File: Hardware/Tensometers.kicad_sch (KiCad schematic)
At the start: 27 parts, among them IC1 MCP1501T-18E_CHY, U24 AD8226BRMZ-R7, U31 MCP6002-xMC, U33 MCP6002-xMC, U34 AD8226BRMZ-R7, U35 AD8226BRMZ-R7, U36 AD8226BRMZ-R7

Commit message: Frontbox 2025 Version 1.0
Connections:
- net 12V1 renamed +12V

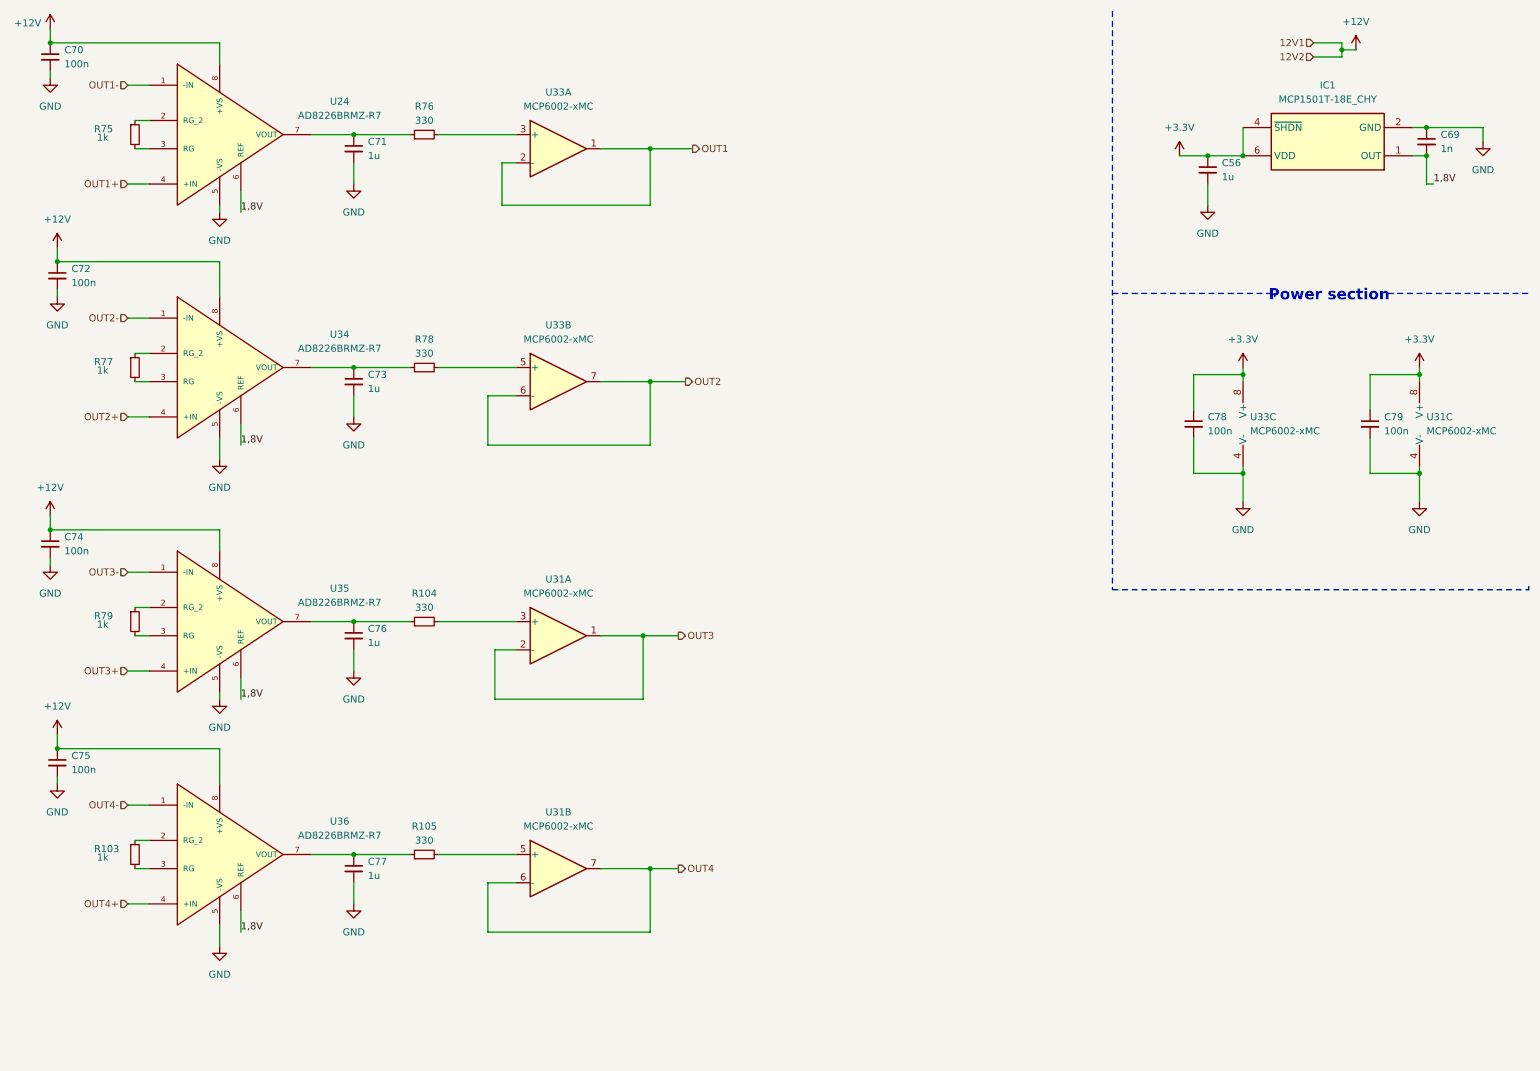
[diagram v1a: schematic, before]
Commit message: Converter change
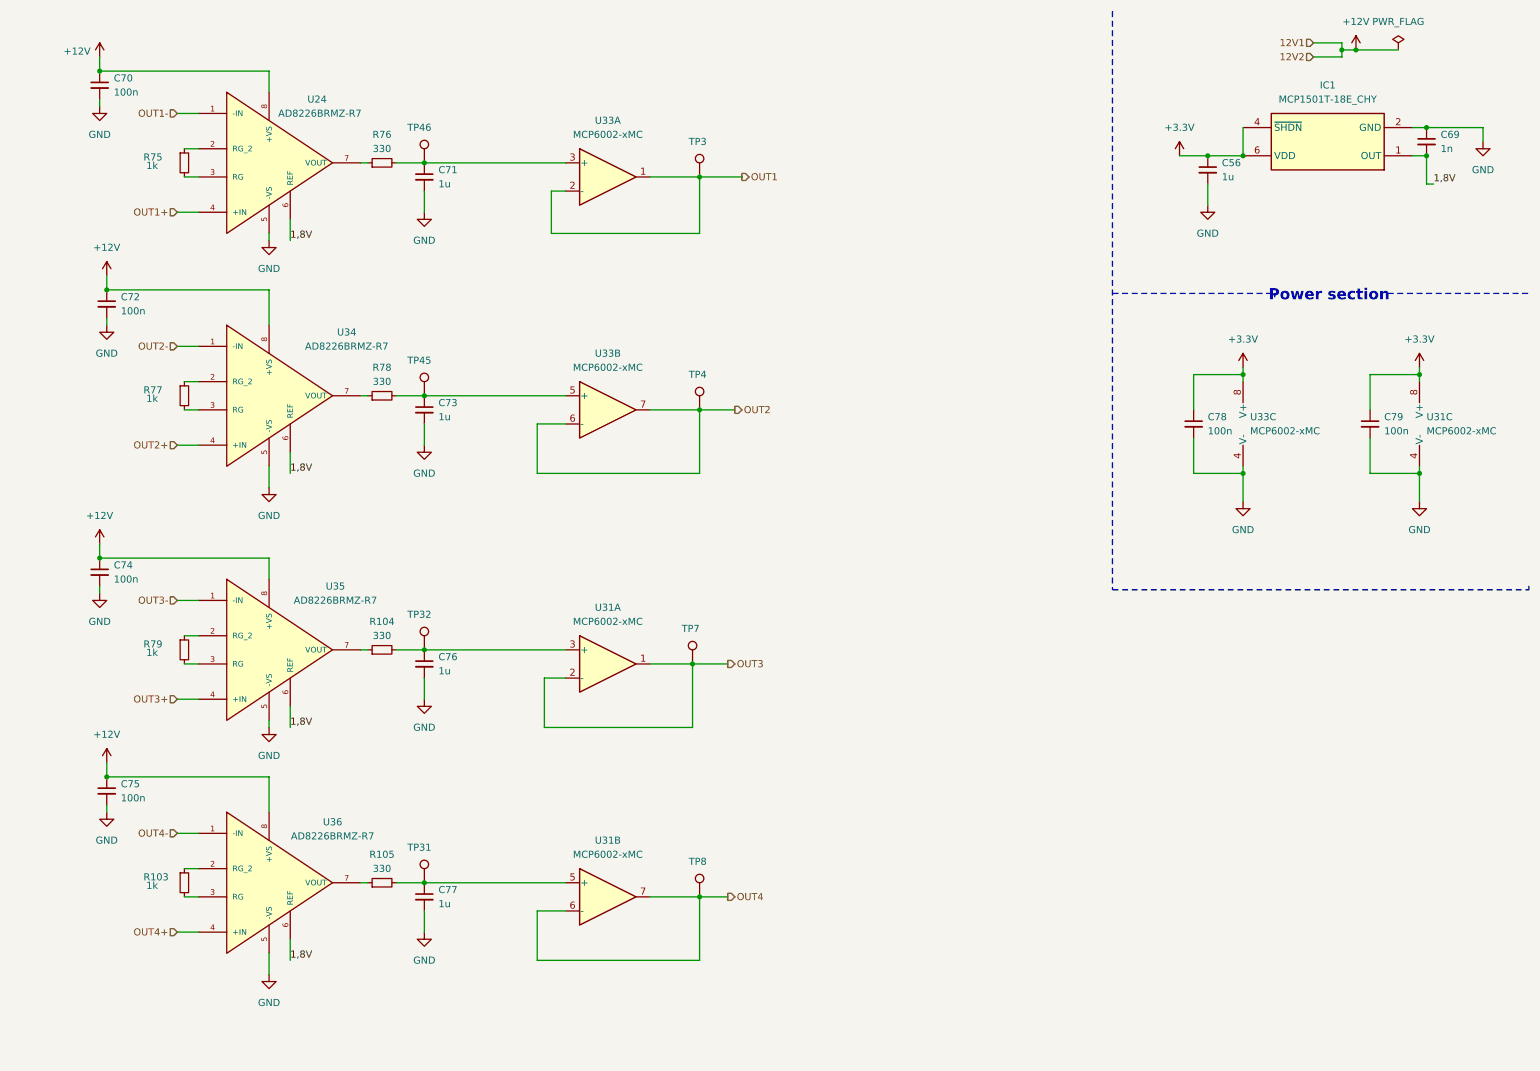
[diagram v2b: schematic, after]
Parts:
- added TP3, TP31, TP32, TP4, TP45, TP46, TP7, TP8: BR_N, TestPoint:TestPoint_THTPad_D1.0mm_Drill0.5mm, symbol Connector:TestPoint
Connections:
- net OUT1: now also TP3.1
- net OUT2: now also TP4.1
- net OUT3: now also TP7.1
- net OUT4: now also TP8.1
- net at R104.1, U35.7 (VOUT): no longer C76.1
- net at R76.1, U24.7 (VOUT): no longer C71.1
- net at R76.2, U33.3 (+): now also C71.1, TP46.1
- net at R78.2, U33.5 (+): now also C73.1, TP45.1
- net at R105.1, U36.7 (VOUT): no longer C77.1
- net at R104.2, U31.3 (+): now also C76.1, TP32.1
- net at R78.1, U34.7 (VOUT): no longer C73.1
- net at R105.2, U31.5 (+): now also C77.1, TP31.1
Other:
- moved on the sheet: C70, C71, C72, C73, C74, C75, C76, C77, R103, R104, R105, R75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

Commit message: Change voltage followers for tensometer to non iverting ampifiers
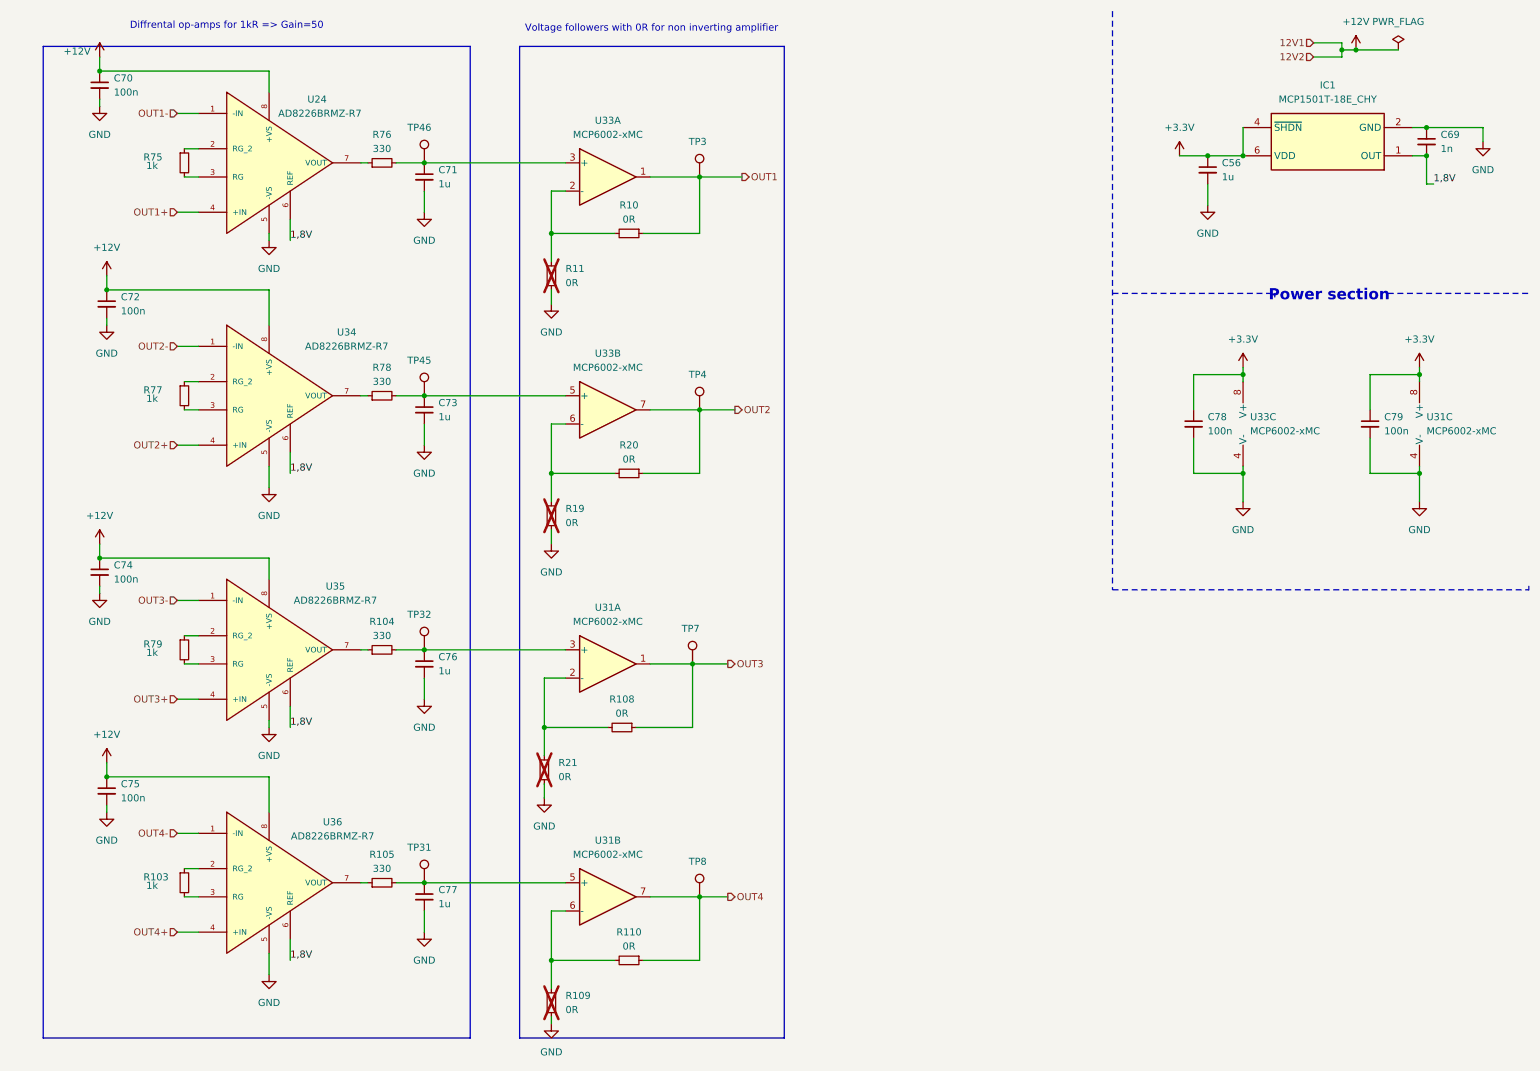
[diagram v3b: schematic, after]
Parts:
- added R10, R108, R109, R11, R110, R19, R20, R21: 0R, Resistor_SMD:R_0603_1608Metric, symbol Device:R_Small
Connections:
- net GND: now also R109.2, R11.2, R19.2, R21.2
- net OUT1: now also R10.1; no longer U33.2 (-)
- net OUT2: now also R20.1; no longer U33.6 (-)
- net OUT3: now also R108.1; no longer U31.2 (-)
- net OUT4: now also R110.1; no longer U31.6 (-)
- new net: R19.1, R20.2, U33.6 (-)
- new net: R109.1, R110.2, U31.6 (-)
- new net: R108.2, R21.1, U31.2 (-)
- new net: R10.2, R11.1, U33.2 (-)
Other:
- note added: "Diffrental op-amps for 1kR => Gain=50"
- note added: "Voltage followers with 0R for non inverting amplifier"

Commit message: Changes in converter layout and tensometers schematic
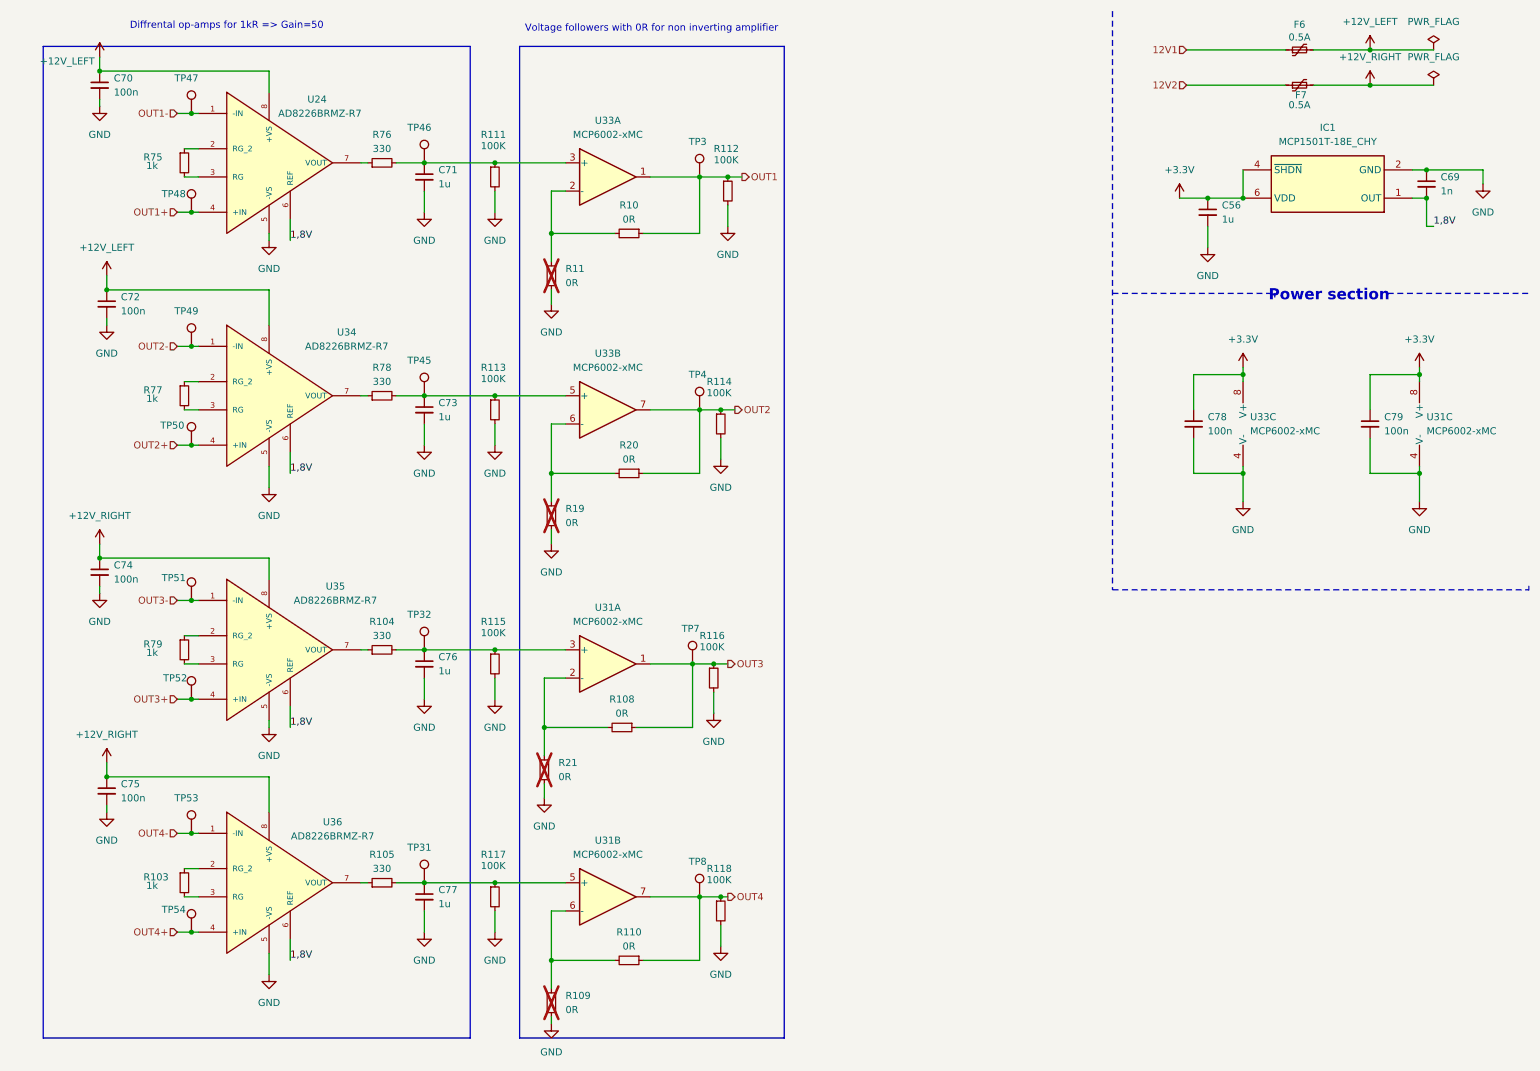
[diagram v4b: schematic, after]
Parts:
- added F6, F7: 0.5A, Fuse:Fuse_0805_2012Metric, symbol Device:Polyfuse_Small
- added R111, R112, R113, R114, R115, R116, R117, R118: 100K, Resistor_SMD:R_0603_1608Metric, symbol Device:R_Small
- added TP47, TP48, TP49, TP50, TP51, TP52, TP53, TP54: BR_N, TestPoint:TestPoint_THTPad_D1.0mm_Drill0.5mm, symbol Connector:TestPoint
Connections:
- net GND: now also R111.2, R112.2, R113.2, R114.2, R115.2, R116.2, R117.2, R118.2
- net OUT1: now also R112.1
- net OUT1+: now also TP48.1
- net OUT1-: now also TP47.1
- net OUT2: now also R114.1
- net OUT2+: now also TP50.1
- net OUT2-: now also TP49.1
- net OUT3: now also R116.1
- net OUT3+: now also TP52.1
- net OUT3-: now also TP51.1
- net OUT4: now also R118.1
- net OUT4+: now also TP54.1
- net OUT4-: now also TP53.1
- net at C76.1, R104.2, TP32.1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: now also R115.1
- net at C71.1, R76.2, TP46.1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: now also R111.1
- net at C73.1, R78.2, TP45.1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: now also R113.1
- net at C77.1, R105.2, TP31.1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: now also R117.1
- net +12V renamed +12V_LEFT
- net +12V_LEFT: now also F6.2; no longer C74.1, C75.1, U35.8 (+VS), U36.8 (+VS)
- new net +12V_RIGHT: C74.1, C75.1, F7.2, U35.8 (+VS), U36.8 (+VS)
- new net 12V1: F6.1
- new net 12V2: F7.1
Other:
- moved on the sheet: C56, C69, IC1

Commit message: Changes Vcc op-amps in brakes pressure (3V3 to 5V) and mcp6002 footprint (to MSOP8)
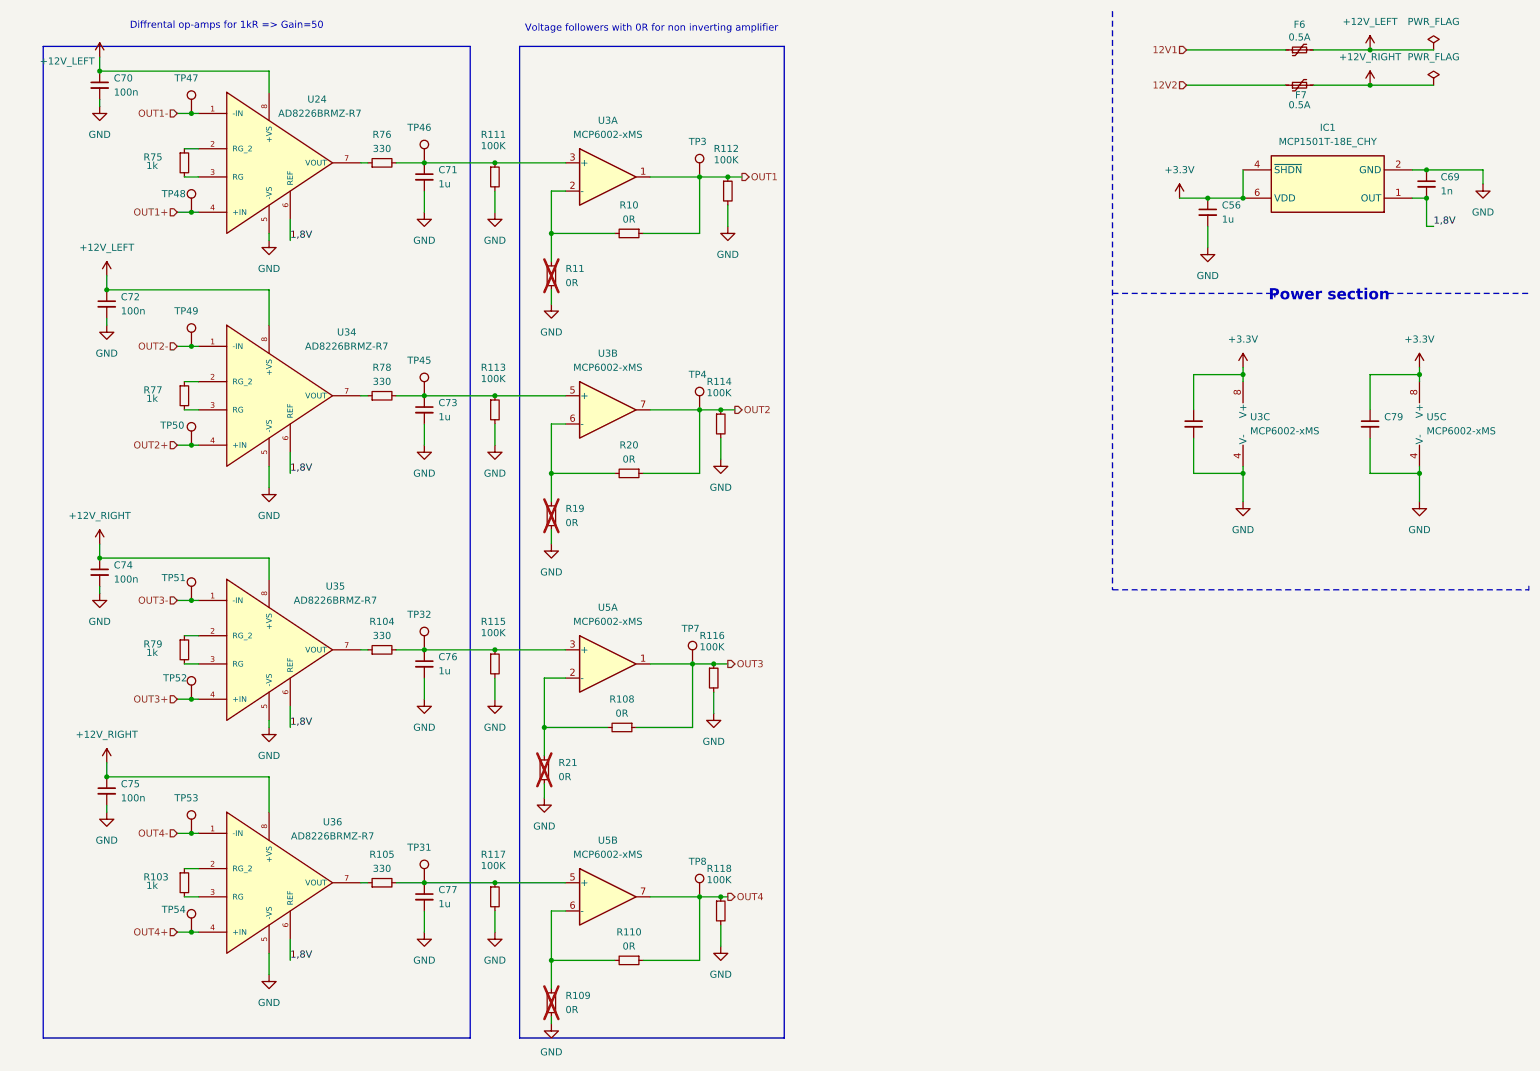
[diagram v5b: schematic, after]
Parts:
- removed U31, U33: MCP6002-xMC, Package_DFN_QFN:DFN-8-1EP_3x2mm_P0.5mm_EP1.75x1.45mm, symbol Amplifier_Operational:MCP6002-xMC
- added U3, U5: MCP6002-xMS, Snapeda:SOP65P490X110-8N, symbol Amplifier_Operational:MCP6002-xMS
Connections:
- net +3.3V: now also U3.8 (V+), U5.8 (V+)
- net GND: now also U3.4 (V-), U5.4 (V-)
- net OUT1: now also U3.1
- net OUT2: now also U3.7
- net OUT3: now also U5.1
- net OUT4: now also U5.7
- net at C76.1, R104.2, R115.1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: now also U5.3 (+)
- net at C71.1, R111.1, R76.2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: now also U3.3 (+)
- net at R19.1, R20.2: now also U3.6 (-)
- net at C73.1, R113.1, R78.2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: now also U3.5 (+)
- net at C77.1, R105.2, R117.1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: now also U5.5 (+)
- net at R109.1, R110.2: now also U5.6 (-)
- net at R108.2, R21.1: now also U5.2 (-)
- net at R10.2, R11.1: now also U3.2 (-)
